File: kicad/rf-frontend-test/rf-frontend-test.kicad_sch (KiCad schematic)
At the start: 26 parts, among them J1 GPIO, J2 SPI, J3 PWR, U1 Si4463, Y1 30MHz

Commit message: clean sch2
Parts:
- U1: footprint Package_DFN_QFN:QFN-20-1EP_4x4mm_P0.5mm_EP2.6x2.6mm_ThermalVias -> Package_DFN_QFN:QFN-20-1EP_4x4mm_P0.5mm_EP2.6x2.6mm
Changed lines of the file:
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@@
 			)
 		)
-		(property "Footprint" "Package_DFN_QFN:QFN-20-1EP_4x4mm_P0.5mm_EP2.6x2.6mm_ThermalVias"
+		(property "Footprint" "Package_DFN_QFN:QFN-20-1EP_4x4mm_P0.5mm_EP2.6x2.6mm"
 			(at 116.84 80.01 0)
 			(effects

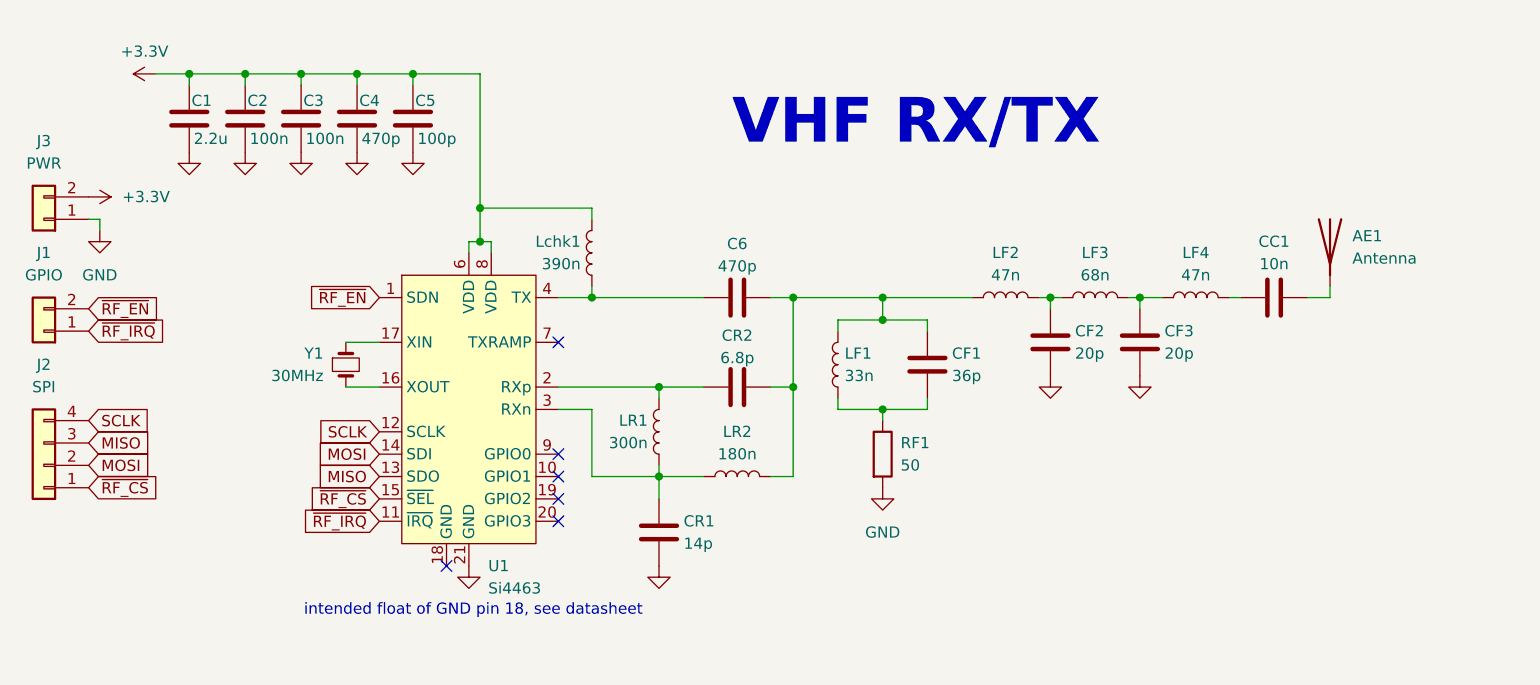
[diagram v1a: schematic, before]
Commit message: Si4463 Transceiver Circuit V2.
Updated the transceiver board to make it compliant with EPL fab limitations. Fixed all GND vias, added Header Pins for the GPIO pins
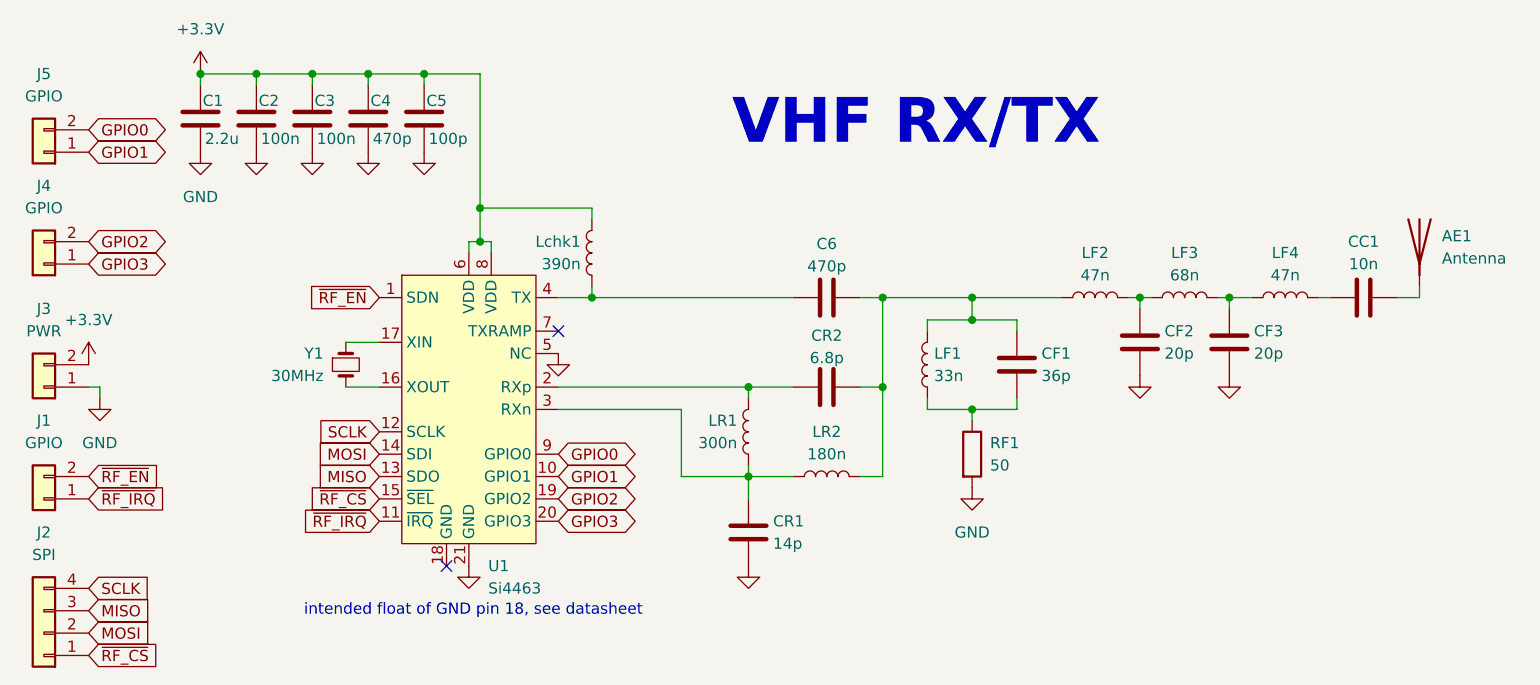
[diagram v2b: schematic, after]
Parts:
- added J4, J5: GPIO, Connector_PinHeader_2.54mm:PinHeader_1x02_P2.54mm_Vertical, symbol Connector_Generic:Conn_01x02
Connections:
- net GND: now also U1.5 (NC)
- net GPIO1: now reaches U1.10 (GPIO1)
- net GPIO1: now also J5.1 (Pin_1)
- net GPIO2: now reaches U1.19 (GPIO2)
- net GPIO2: now also J4.2 (Pin_2)
- net GPIO3: now reaches U1.20 (GPIO3)
- net GPIO3: now also J4.1 (Pin_1)
- net GPIO0: now reaches U1.9 (GPIO0)
- net GPIO0: now also J5.2 (Pin_2)
- no-connect marks 6 -> 2
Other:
- moved on the sheet: AE1, C1, C2, C3, C4, C5, C6, CC1, CF1, CF2, CF3, CR1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

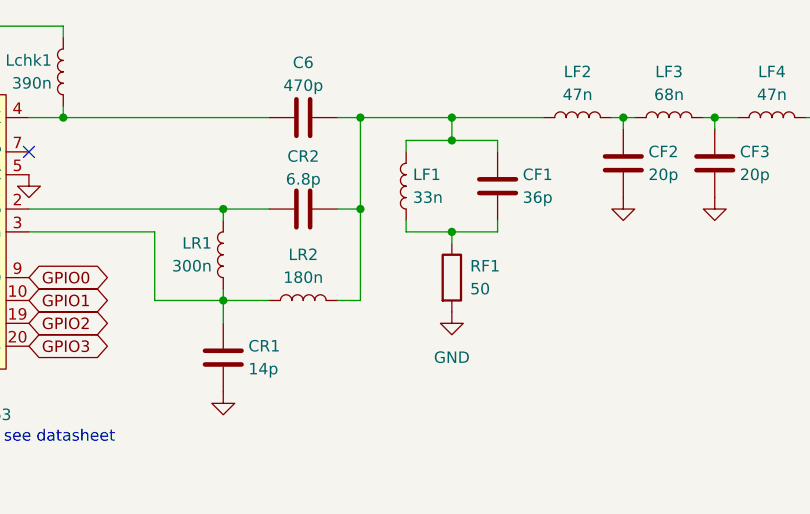
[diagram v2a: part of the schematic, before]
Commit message: slight value changes to rf frontend
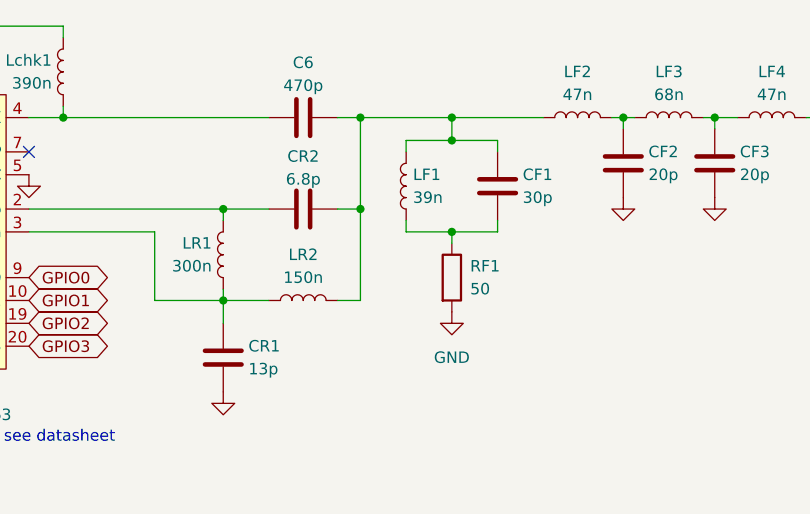
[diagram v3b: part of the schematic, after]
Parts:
- CF1: value 36p -> 30p
- CR1: value 14p -> 13p
- LF1: value 33n -> 39n
- LR2: value 180n -> 150n
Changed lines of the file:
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@@
 			)
 		)
-		(property "Value" "36p"
+		(property "Value" "30p"
 			(at 181.864 106.68 0)
 			(effects
@@
 			)
 		)
-		(property "Value" "180n"
+		(property "Value" "150n"
 			(at 157.48 115.57 90)
 			(effects
@@
 			)
 		)
-		(property "Value" "33n"
+		(property "Value" "39n"
 			(at 169.672 106.68 0)
 			(effects
@@
 			)
 		)
-		(property "Value" "14p"
+		(property "Value" "13p"
 			(at 151.384 125.73 0)
 			(effects
